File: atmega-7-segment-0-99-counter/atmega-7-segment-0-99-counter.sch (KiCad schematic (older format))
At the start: 56 parts, among them Q1 PN2222A, Q2 PN2222A

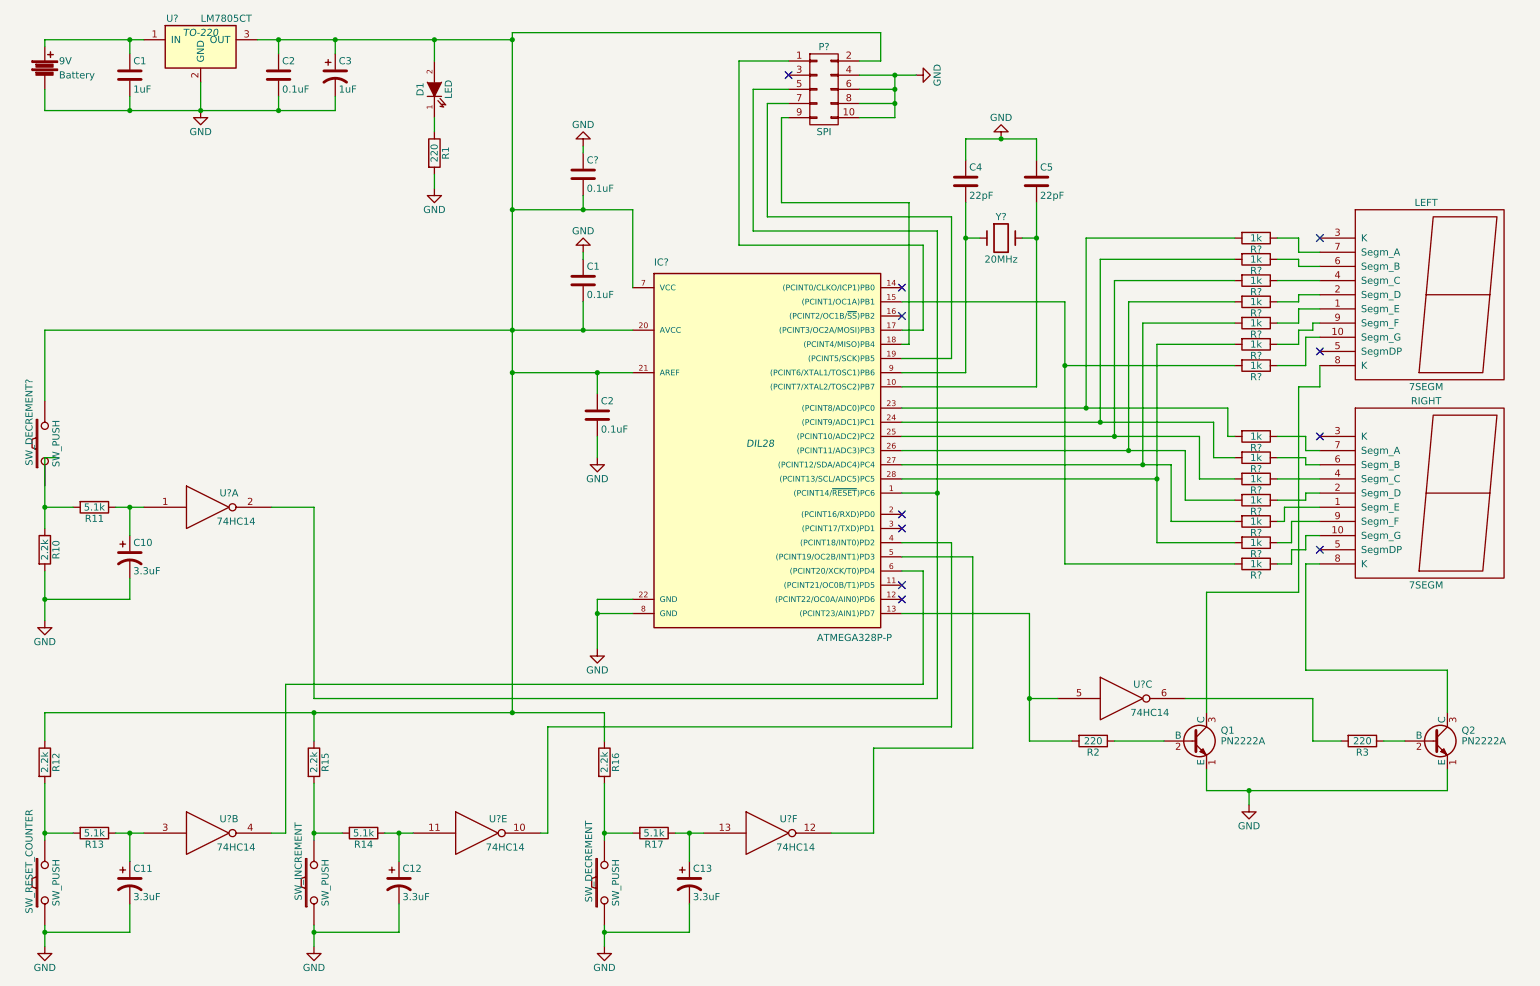
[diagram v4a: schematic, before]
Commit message: Moved from A4 to letter + fixed labels
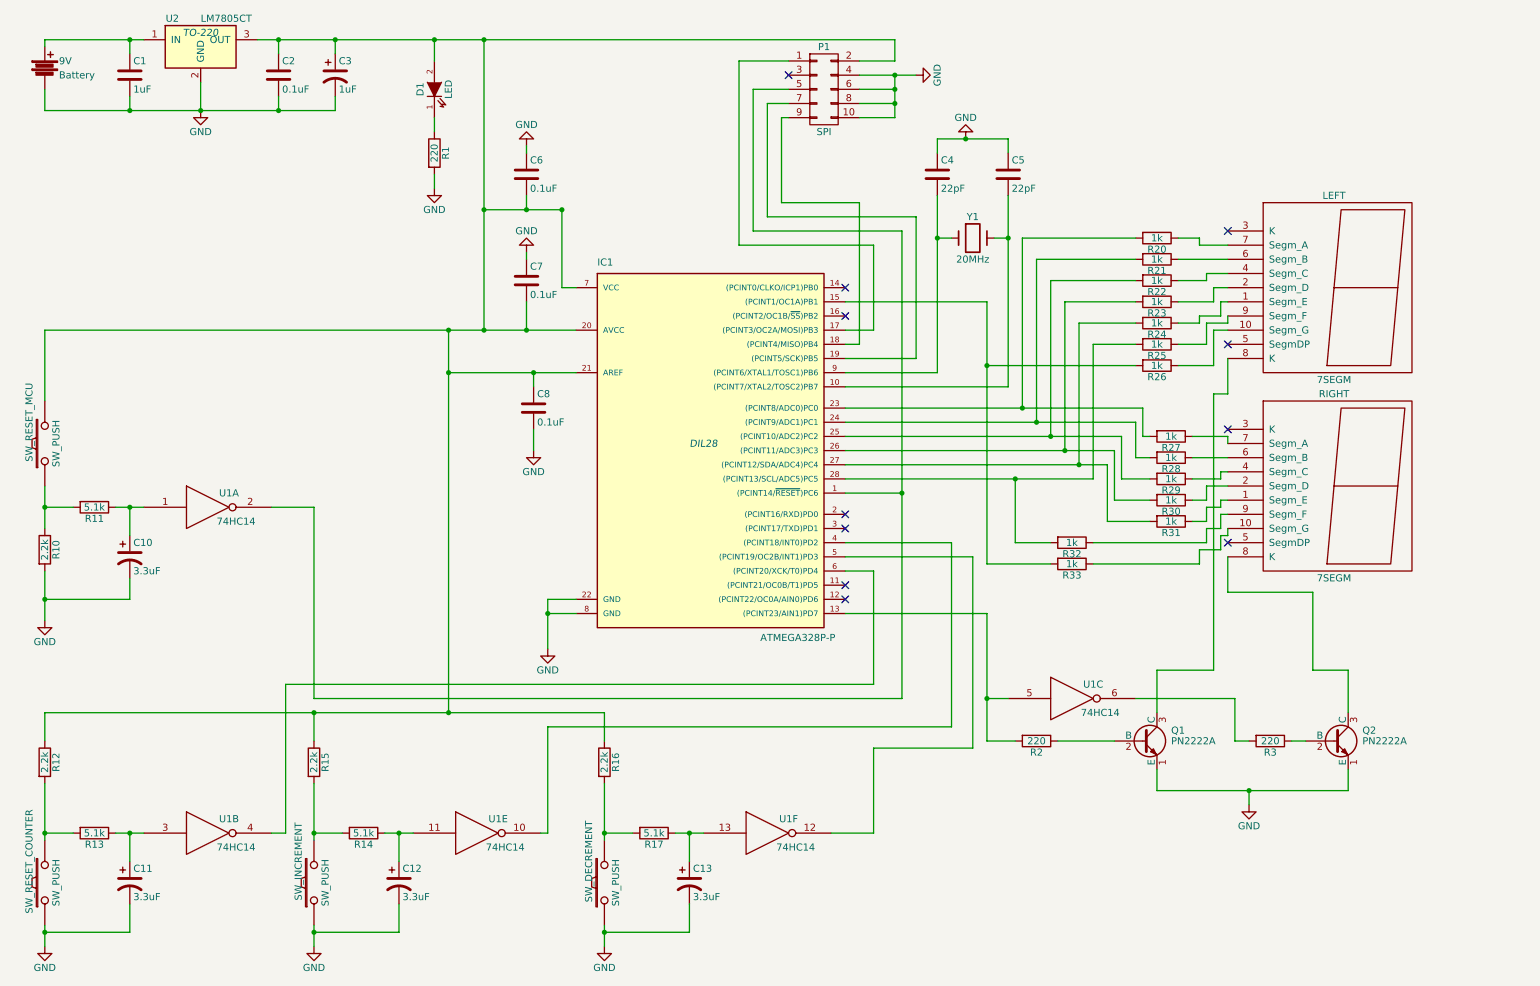
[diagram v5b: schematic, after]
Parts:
- gave numbers to parts that had none: 21
- renumbered C1 to C7, C2 to C8
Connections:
- net at SW_RESET_MCU.1: now also R10.1, R11.2
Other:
- moved on the sheet: C4, C5, C6, C7, C8, IC1, LEFT, Q1, Q2, R2, R20, R21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

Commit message: Fixed toggle Inverter for displays + regenerated PDF
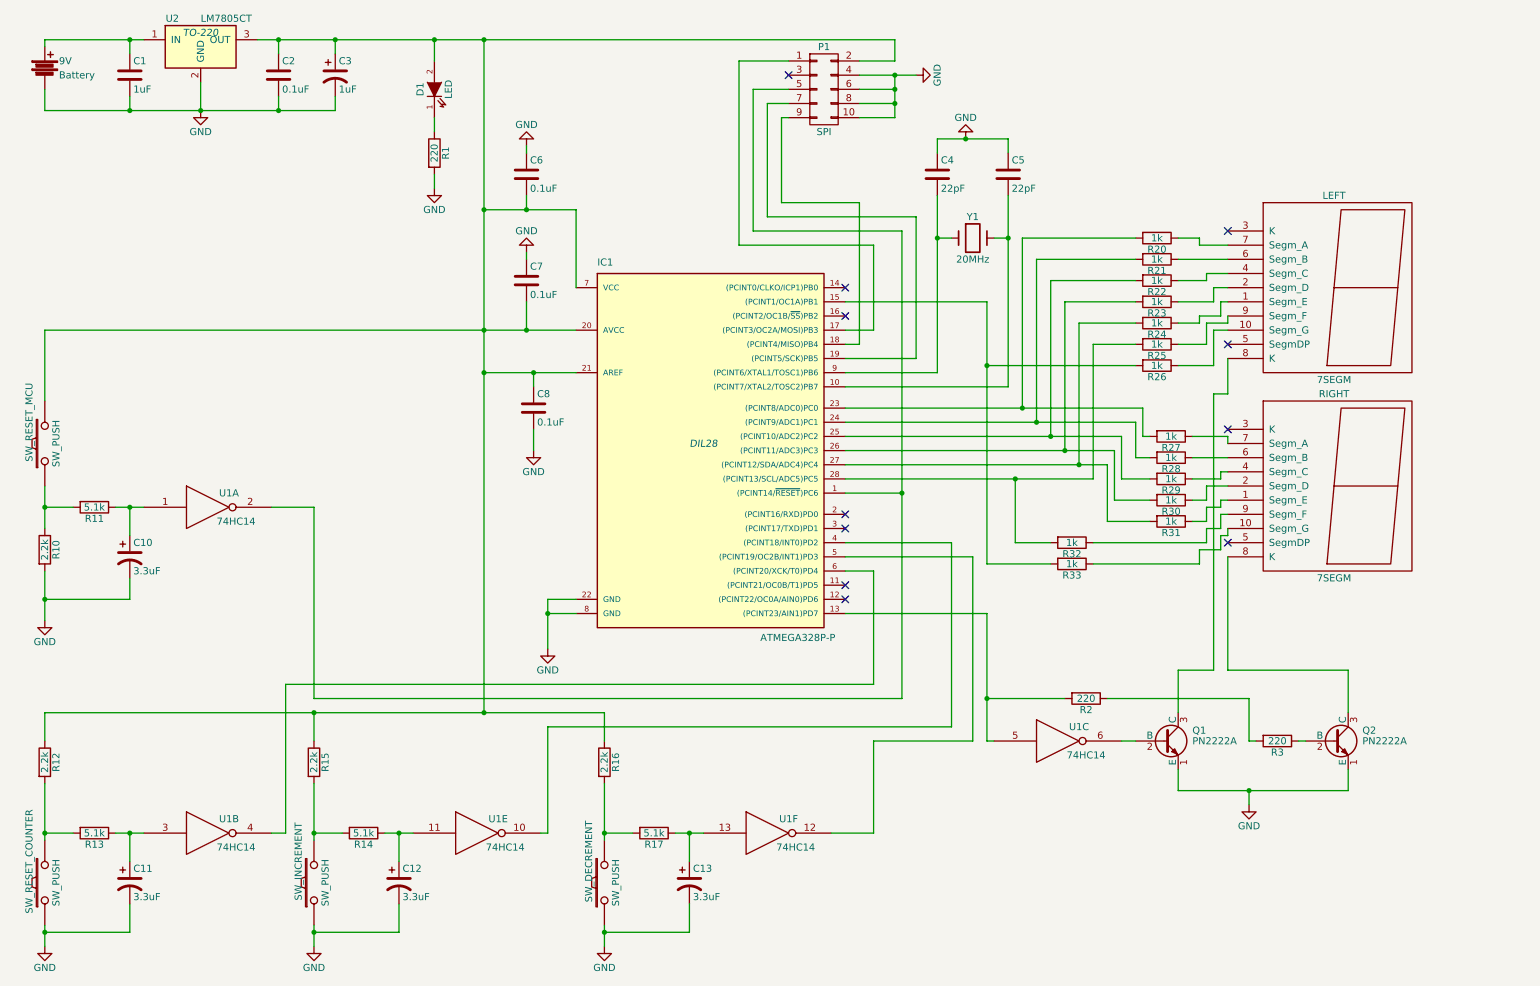
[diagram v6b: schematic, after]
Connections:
- net at Q1.2 (B): now also U1.6; no longer R2.1
- net at R3.2: now also R2.1; no longer U1.6
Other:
- moved on the sheet: Q1, R2, R3, U1C
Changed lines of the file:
@@
 Rev "v1"
 Comp "SINGSONN"
-Comment1 ""
+Comment1 "https://github.com/singsonn/atmega-two-7-segment-counter"
 Comment2 ""
 Comment3 ""
@@
 L PN2222A Q1
 U 1 1 57D04261
-P 8550 5800
-F 0 "Q1" H 8750 5875 50  0000 L CNN
-F 1 "PN2222A" H 8750 5800 50  0000 L CNN
-F 2 "" H 8750 5725 50  0000 L CIN
-F 3 "" H 8550 5800 50  0000 L CNN
-	1    8550 5800
+P 8700 5800
+F 0 "Q1" H 8900 5875 50  0000 L CNN
+F 1 "PN2222A" H 8900 5800 50  0000 L CNN
+F 2 "" H 8900 5725 50  0000 L CIN
+F 3 "" H 8700 5800 50  0000 L CNN
+	1    8700 5800
 	1    0    0    -1
 $EndComp
@@
 L 74HC14 U1
 U 3 1 57D087BB
-P 8050 5500
-F 0 "U1" H 8200 5600 50  0000 C CNN
-F 1 "74HC14" H 8250 5400 50  0000 C CNN
-F 2 "" H 8050 5500 50  0000 C CNN
-F 3 "" H 8050 5500 50  0000 C CNN
-	3    8050 5500
+P 7950 5800
+F 0 "U1" H 8100 5900 50  0000 C CNN
+F 1 "74HC14" H 8150 5700 50  0000 C CNN
+F 2 "" H 7950 5800 50  0000 C CNN
+F 3 "" H 7950 5800 50  0000 C CNN
+	3    7950 5800
 	1    0    0    -1
 $EndComp
@@
 L R R2
 U 1 1 57D108BD
-P 7800 5800
-F 0 "R2" V 7880 5800 50  0000 C CNN
-F 1 "220" V 7800 5800 50  0000 C CNN
-F 2 "" V 7730 5800 50  0000 C CNN
-F 3 "" H 7800 5800 50  0000 C CNN
-	1    7800 5800
+P 8150 5500
+F 0 "R2" V 8230 5500 50  0000 C CNN
+F 1 "220" V 8150 5500 50  0000 C CNN
+F 2 "" V 8080 5500 50  0000 C CNN
+F 3 "" H 8150 5500 50  0000 C CNN
+	1    8150 5500
 	0    1    1    0
 $EndComp
@@
 L R R3
 U 1 1 57D10FFC
-P 9450 5800
-F 0 "R3" V 9530 5800 50  0000 C CNN
-F 1 "220" V 9450 5800 50  0000 C CNN
-F 2 "" V 9380 5800 50  0000 C CNN
-F 3 "" H 9450 5800 50  0000 C CNN
-	1    9450 5800
+P 9500 5800
+F 0 "R3" V 9580 5800 50  0000 C CNN
+F 1 "220" V 9500 5800 50  0000 C CNN
+F 2 "" V 9430 5800 50  0000 C CNN
+F 3 "" H 9500 5800 50  0000 C CNN
+	1    9500 5800
 	0    1    1    0
 $EndComp
@@
 	3900 850  6800 850
 Wire Wire Line
-	3650 5600 3650 3200
-Wire Wire Line
-	3650 3200 3650 2900
+	3900 5600 3900 3200
+Wire Wire Line
+	3900 3200 3900 2900
 Wire Wire Line
 	3900 2900 3900 2050
@@
 	3900 2050 3900 850
 Wire Wire Line
-	3650 3200 4250 3200
+	3900 3200 4250 3200
 Wire Wire Line
 	4250 3200 4550 3200
 Wire Wire Line
-	800  2900 3650 2900
-Wire Wire Line
-	3650 2900 3900 2900
+	800  2900 3900 2900
 Wire Wire Line
 	3900 2900 4200 2900
@@
 	3900 2050 4200 2050
 Wire Wire Line
-	4200 2050 4450 2050
+	4200 2050 4550 2050
 Wire Wire Line
 	4250 3300 4250 3200
 Connection ~ 4250 3200
 Wire Wire Line
-	4200 1950 4200 2050
-Connection ~ 4200 2050
+	4200 2050 4200 1950
 Wire Wire Line
 	4250 3600 4250 3750
@@
 	1400 6650 1400 6450
 Connection ~ 1400 6450
-Connection ~ 3650 3200
+Connection ~ 3900 3200
 Wire Wire Line
 	1400 6950 1400 7150
@@
 	6850 4050 6850 5500
 Wire Wire Line
-	8650 6000 8650 6150
-Wire Wire Line
-	8650 6150 9300 6150
+	8800 6000 8800 6150
+Wire Wire Line
+	8800 6150 9300 6150
 Wire Wire Line
 	9300 6150 10000 6150
@@
 Connection ~ 9300 6150
 Wire Wire Line
-	9750 5300 10000 5300
+	9150 5300 10000 5300
 Connection ~ 3900 2050
 Wire Wire Line
@@
 	800  5600 2700 5600
 Wire Wire Line
-	2700 5600 3650 5600
-Wire Wire Line
-	3650 5600 4750 5600
+	2700 5600 3900 5600
+Wire Wire Line
+	3900 5600 4750 5600
 Wire Wire Line
 	2700 5600 2700 5800
@@
 Wire Wire Line
 	4750 5600 4750 5800
-Connection ~ 3650 5600
+Connection ~ 3900 5600
 Wire Wire Line
 	2700 4150 2700 5500
@@
 	6350 6450 6650 6450
 Wire Wire Line
-	6650 6450 6650 5850
-Wire Wire Line
-	6650 5850 7350 5850
-Wire Wire Line
-	7350 5850 7350 4500
+	6650 6450 6650 5800
+Wire Wire Line
+	6650 5800 7350 5800
+Wire Wire Line
+	7350 5800 7350 4500
 Wire Wire Line
 	7350 4500 6450 4500
@@
 	6650 4600 6450 4600
 Wire Wire Line
-	9600 5800 9700 5800
+	9650 5800 9700 5800
 Wire Wire Line
 	10000 5300 10000 5600
@@
 Wire Wire Line
 	7600 2250 7500 2250
-Wire Wire Line
-	7100 1650 7100 1550
 Wire Wire Line
 	7600 1550 7600 1650
@@
 Connection ~ 8100 3850
 Wire Wire Line
-	8650 5600 8650 5300
-Wire Wire Line
-	8650 5300 9050 5300
+	8800 5600 8800 5300
+Wire Wire Line
+	8800 5300 9050 5300
 Wire Wire Line
 	800  850  800  900
@@
 	800  1350 800  1200
 Wire Wire Line
-	7450 5500 7600 5500
-Wire Wire Line
-	9300 5800 9200 5800
-Wire Wire Line
-	9200 5800 9200 5500
-Wire Wire Line
-	9200 5500 8500 5500
-Wire Wire Line
-	7950 5800 8350 5800
-Wire Wire Line
-	7450 5800 7650 5800
+	7450 5500 8000 5500
+Wire Wire Line
+	9350 5800 9300 5800
+Wire Wire Line
+	9300 5800 9300 5500
+Wire Wire Line
+	9300 5500 8300 5500
 Wire Wire Line
 	6550 1000 6800 1000
@@
 Connection ~ 7650 3950
 Wire Wire Line
-	9750 5300 9750 4750
-Wire Wire Line
-	9750 4750 9150 4750
-Wire Wire Line
-	9150 4750 9150 4500
+	9150 5300 9150 4500
 Wire Wire Line
 	9000 4000 9150 4000
@@
 Wire Wire Line
 	9000 4100 8900 4100
-Connection ~ 3650 2900
-Wire Wire Line
-	4550 2600 4450 2600
-Wire Wire Line
-	4450 2600 4450 2050
-Connection ~ 4450 2050
+Wire Wire Line
+	4550 2050 4550 2600
+Connection ~ 4200 2050
+Wire Wire Line
+	7100 1550 7100 1650
+Wire Wire Line
+	7450 5800 7500 5800
+Wire Wire Line
+	8400 5800 8500 5800
 $EndSCHEMATC

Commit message: Fixed wiring issues to 2N2222s
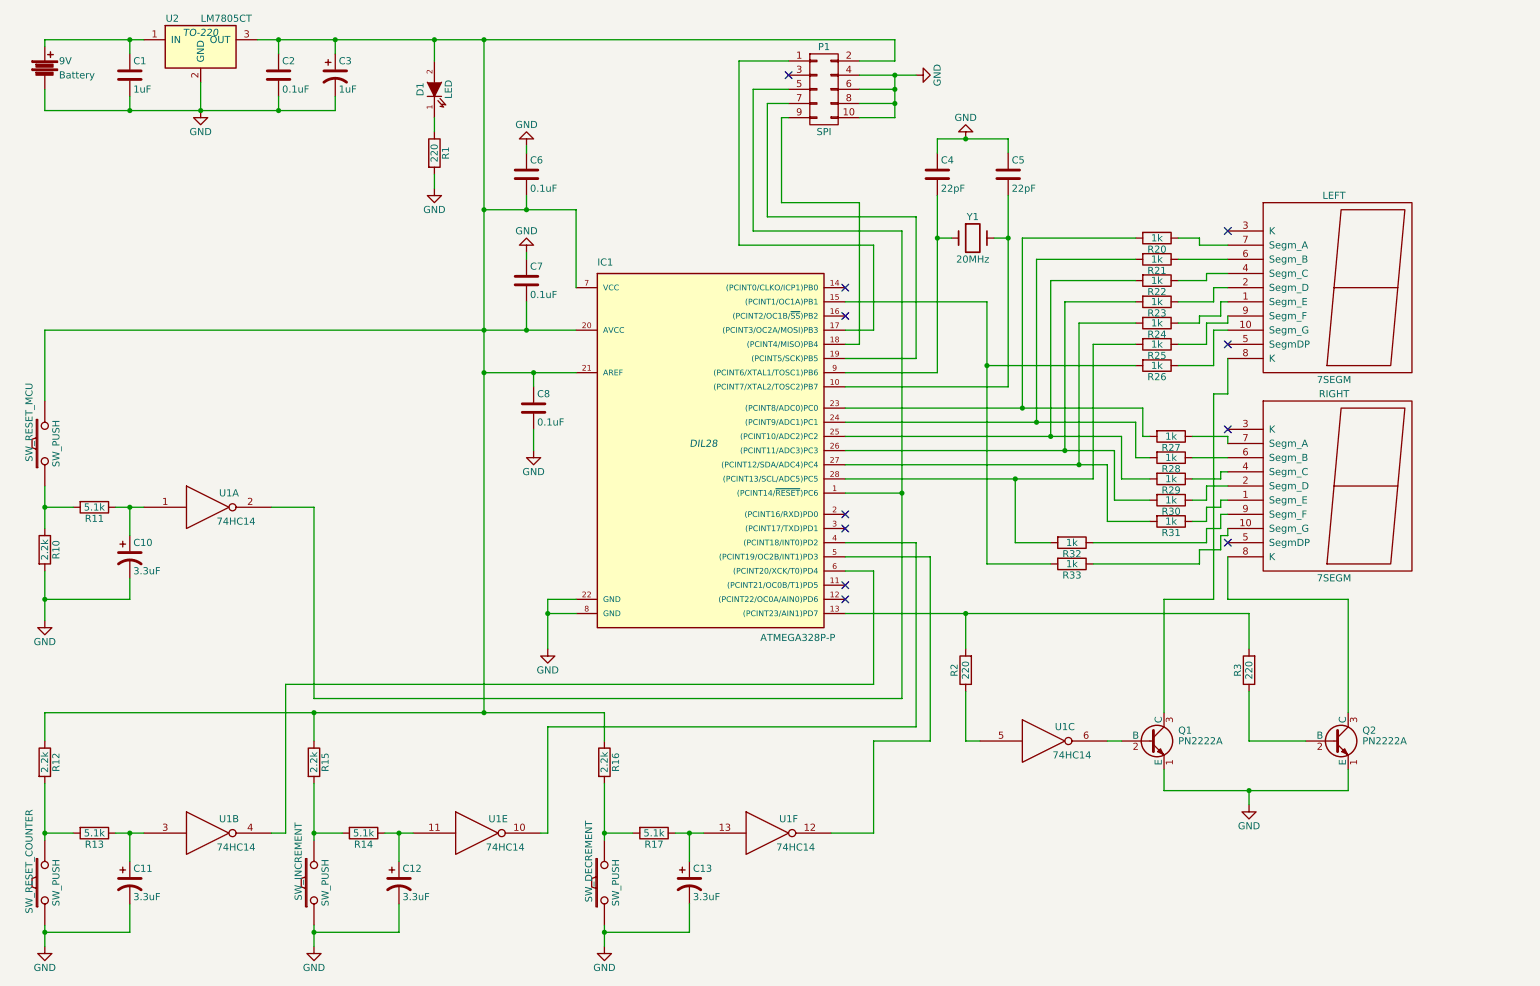
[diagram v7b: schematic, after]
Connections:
- net at IC1.13 ((PCINT23/AIN1)PD7), R2.2: now also R3.2; no longer U1.5
- net at R2.1: now also U1.5; no longer R3.2
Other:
- moved on the sheet: Q1, R2, R3, U1C

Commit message: Fixed Resistors placement for transistors
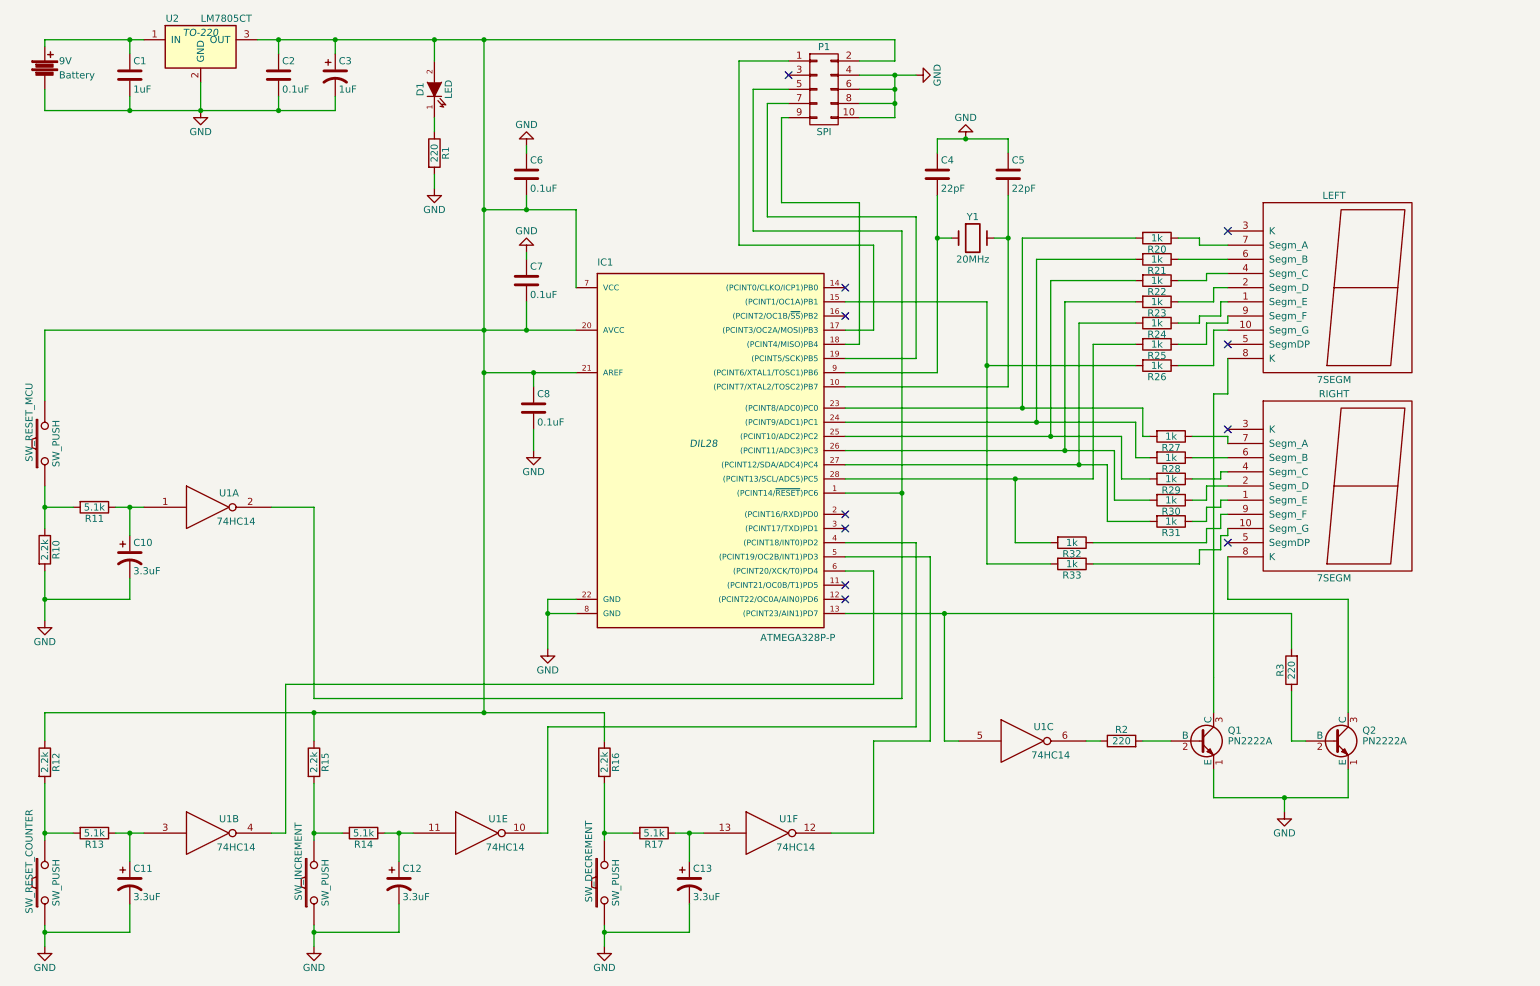
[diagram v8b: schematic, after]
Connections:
- net at IC1.13 ((PCINT23/AIN1)PD7), R3.2: now also U1.5; no longer R2.2
- net at Q1.2 (B): now also R2.2; no longer U1.6
- net at R2.1: now also U1.6; no longer U1.5
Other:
- moved on the sheet: Q1, R2, R3, U1C
